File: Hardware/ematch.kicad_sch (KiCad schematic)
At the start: 34 parts, among them J3 Conn_01x02_Male, J4 Conn_01x02_Male, J5 Conn_01x02_Male, J6 Conn_01x02_Male, Q1 PMV20ENR, Q2 PMV20ENR, Q3 PMV20ENR, Q4 PMV20ENR, U6 LTV-247

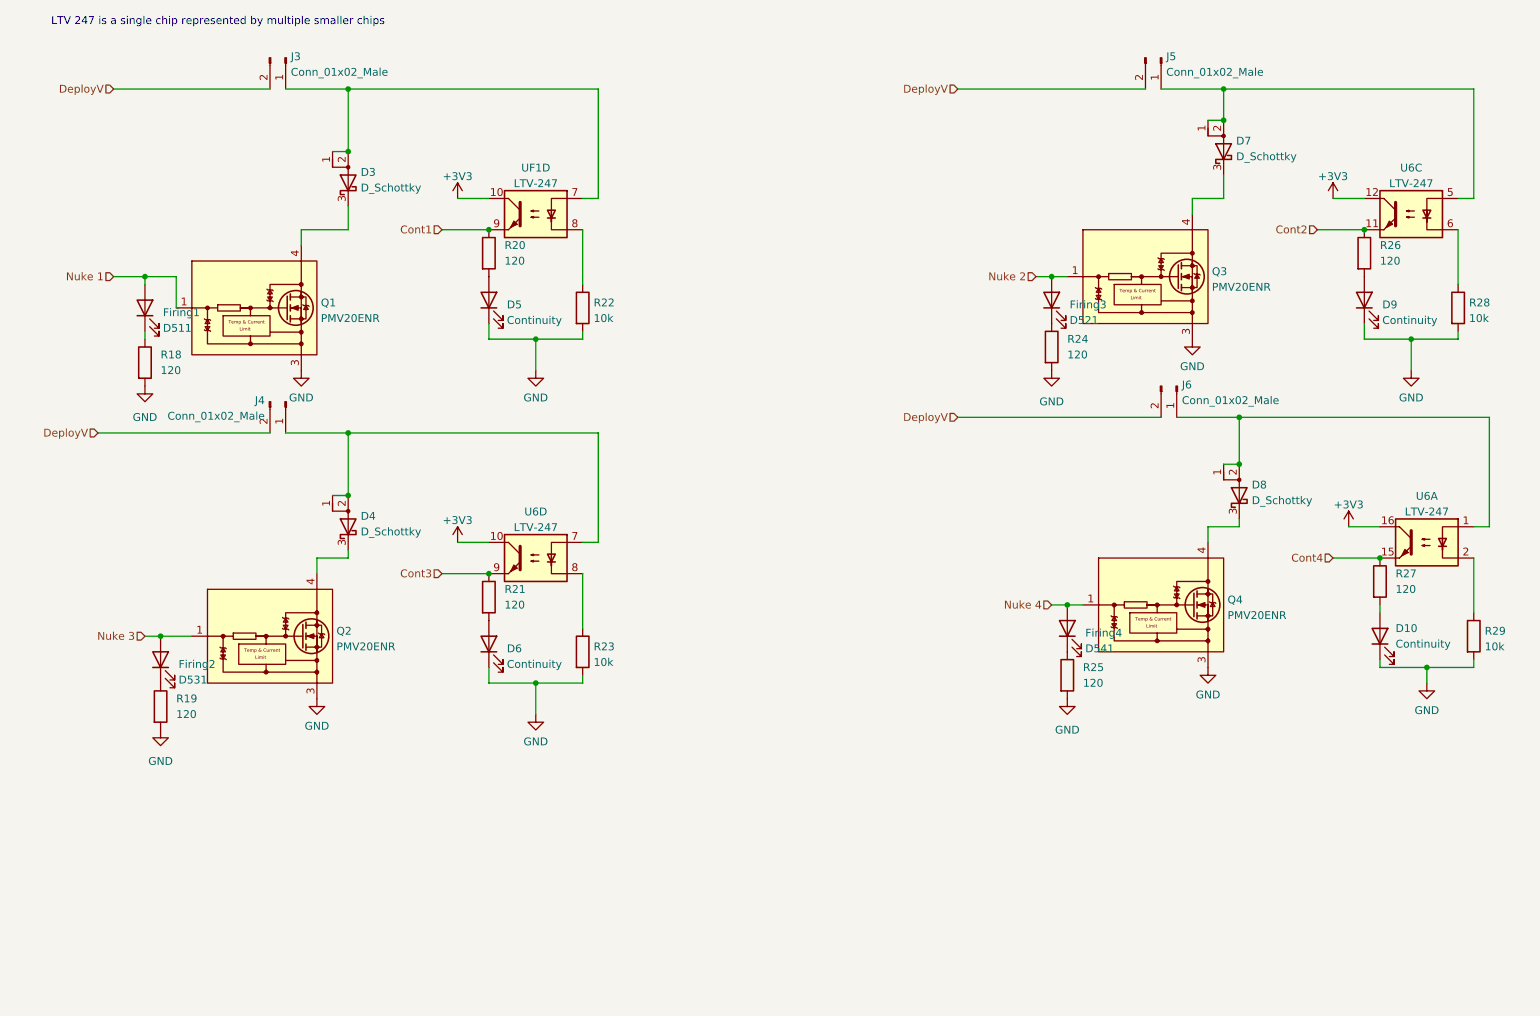
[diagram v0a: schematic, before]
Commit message: schematic done? + footprints assigned
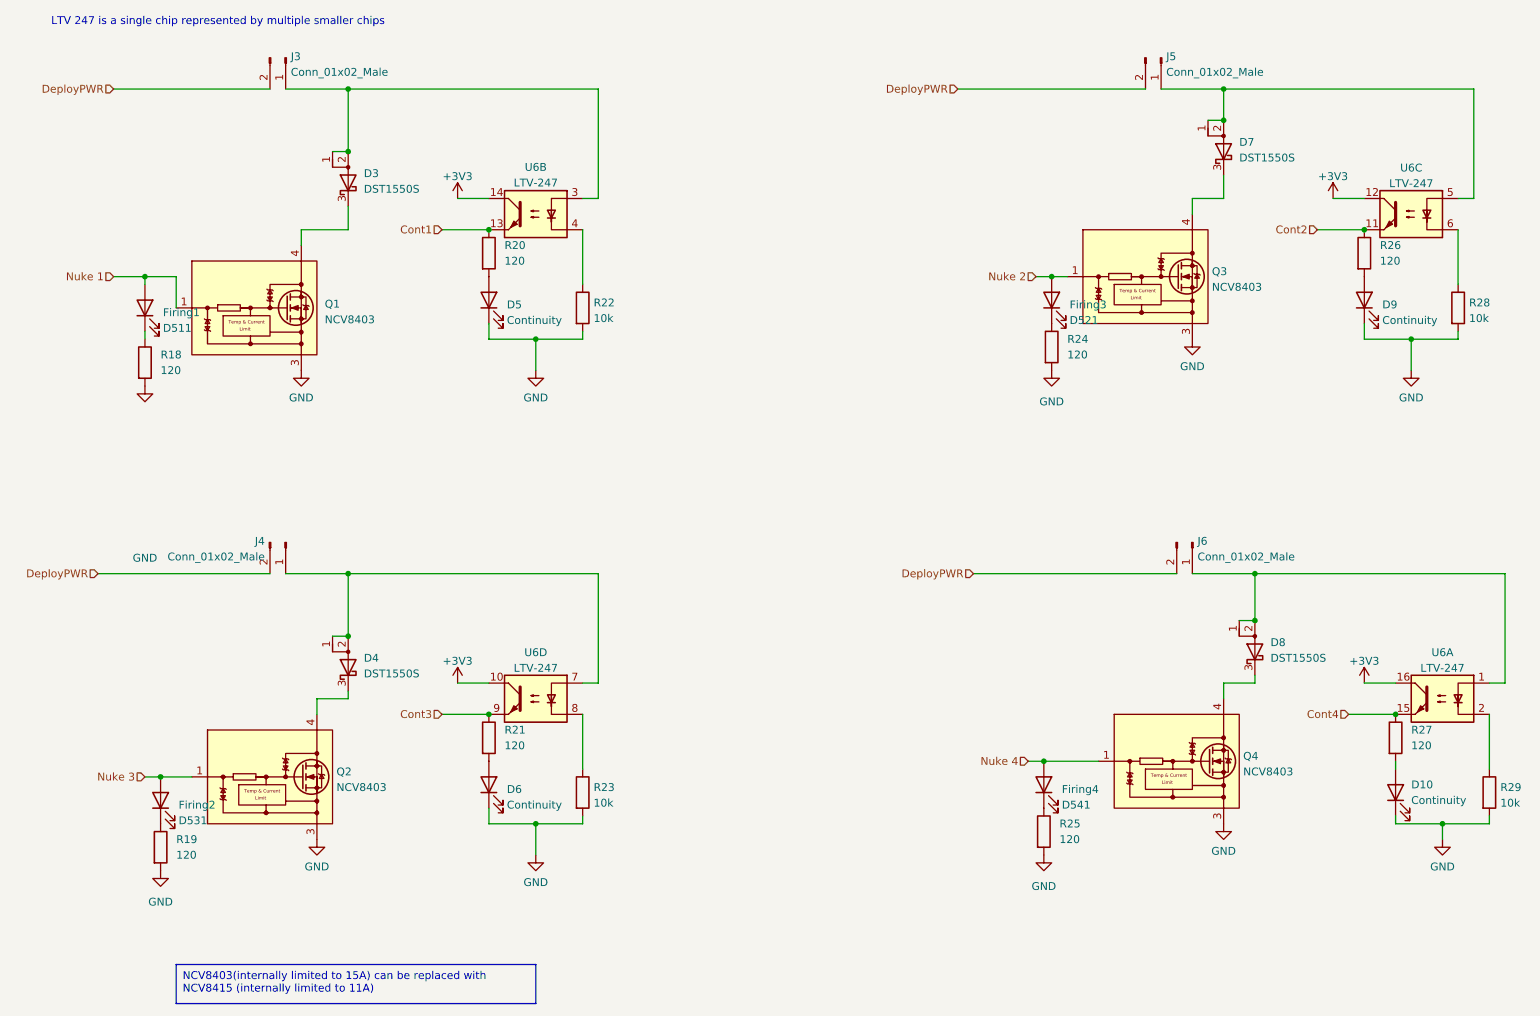
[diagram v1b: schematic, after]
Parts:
- D3, D4, D7, D8: value D_Schottky -> DST1550S
- Q1, Q2, Q3, Q4: value PMV20ENR -> NCV8403
- renumbered UF1 to U6
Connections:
- net +3V3: now also U6.14; no longer U6.10
- net Cont1: now also U6.13; no longer U6.9
- net at D3.1 (A), D3.2 (A), J3.1 (Pin_1): now also U6.3; no longer U6.7
- net at R22.1: now also U6.4; no longer U6.8
- net DeployV renamed DeployPWR
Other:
- moved on the sheet: D10, D4, D6, D8, Firing2, Firing4, J4, J6, Q2, Q4, R19, R21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

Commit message: High power side nearly done
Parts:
- J3, J4, J5, J6: footprint TerminalBlock_TE-Connectivity:TerminalBlock_TE_282834-2_1x02_P2.54mm_Horizontal -> TerminalBlock_Phoenix:TerminalBlock_Phoenix_PT-1,5-2-3.5-H_1x02_P3.50mm_Horizontal
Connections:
- net DeployPWR: now also J3.1 (Pin_1), J4.1 (Pin_1), J5.1 (Pin_1), J6.1 (Pin_1); no longer J3.2 (Pin_2), J4.2 (Pin_2), J5.2 (Pin_2), J6.2 (Pin_2)
- net at D3.1 (A), D3.2 (A), U6.3: now also J3.2 (Pin_2); no longer J3.1 (Pin_1)
- net at D4.1 (A), D4.2 (A), U6.7: now also J4.2 (Pin_2); no longer J4.1 (Pin_1)
- net at D8.1 (A), D8.2 (A), U6.1: now also J6.2 (Pin_2); no longer J6.1 (Pin_1)
- net at D7.1 (A), D7.2 (A), U6.5: now also J5.2 (Pin_2); no longer J5.1 (Pin_1)
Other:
- moved on the sheet: J3, J4, J5, J6
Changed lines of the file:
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@@
-    (stroke (width 0) (type default))
-  )
-  (wire (pts (xy 203.2 109.22) (xy 213.36 109.22))
     (stroke (width 0) (type default))
   )
@@
     (stroke (width 0) (type default))
   )
-  (wire (pts (xy 198.12 30.48) (xy 208.28 30.48))
-    (stroke (width 0) (type default))
-  )
   (wire (pts (xy 251.46 132.08) (xy 251.46 140.97))
     (stroke (width 0) (type default))
@@
     (stroke (width 0) (type default))
   )
+  (wire (pts (xy 58.42 109.22) (xy 66.04 109.22))
+    (stroke (width 0) (type default))
+  )
   (wire (pts (xy 238.76 71.12) (xy 246.38 71.12))
     (stroke (width 0) (type default))
@@
     (stroke (width 0) (type default))
   )
-  (wire (pts (xy 165.1 30.48) (xy 195.58 30.48))
-    (stroke (width 0) (type default))
-  )
   (wire (pts (xy 213.36 109.22) (xy 254 109.22))
     (stroke (width 0) (type default))
@@
     (stroke (width 0) (type default))
   )
+  (wire (pts (xy 205.74 109.22) (xy 213.36 109.22))
+    (stroke (width 0) (type default))
+  )
   (wire (pts (xy 58.42 53.34) (xy 58.42 55.88))
     (stroke (width 0) (type default))
@@
     (stroke (width 0) (type default))
   )
-  (wire (pts (xy 167.64 109.22) (xy 200.66 109.22))
-    (stroke (width 0) (type default))
-  )
-  (wire (pts (xy 55.88 109.22) (xy 66.04 109.22))
+  (wire (pts (xy 167.64 109.22) (xy 203.2 109.22))
     (stroke (width 0) (type default))
   )
@@
     (stroke (width 0) (type default))
   )
-  (wire (pts (xy 27.94 30.48) (xy 53.34 30.48))
+  (wire (pts (xy 27.94 30.48) (xy 55.88 30.48))
     (stroke (width 0) (type default))
   )
@@
     (stroke (width 0) (type default))
   )
+  (wire (pts (xy 200.66 30.48) (xy 208.28 30.48))
+    (stroke (width 0) (type default))
+  )
   (wire (pts (xy 88.9 149.86) (xy 96.52 149.86))
     (stroke (width 0) (type default))
@@
     (stroke (width 0) (type default))
   )
+  (wire (pts (xy 58.42 30.48) (xy 66.04 30.48))
+    (stroke (width 0) (type default))
+  )
   (wire (pts (xy 104.14 132.08) (xy 104.14 140.97))
     (stroke (width 0) (type default))
@@
     (stroke (width 0) (type default))
   )
-  (wire (pts (xy 25.4 109.22) (xy 53.34 109.22))
+  (wire (pts (xy 25.4 109.22) (xy 55.88 109.22))
     (stroke (width 0) (type default))
   )
@@
     (stroke (width 0) (type default))
   )
-  (wire (pts (xy 55.88 30.48) (xy 66.04 30.48))
-    (stroke (width 0) (type default))
-  )
   (wire (pts (xy 63.5 119.38) (xy 66.04 119.38))
     (stroke (width 0) (type default))
   )
   (wire (pts (xy 228.6 132.08) (xy 236.22 132.08))
+    (stroke (width 0) (type default))
+  )
+  (wire (pts (xy 165.1 30.48) (xy 198.12 30.48))
     (stroke (width 0) (type default))
   )
@@
     )
   )
-  (symbol (lib_id "Connector:Conn_01x02_Male") (at 55.88 25.4 270) (unit 1)
-    (in_bom yes) (on_board yes) (dnp no) (fields_autoplaced)
-    (property "Reference" "J3" (at 56.7182 25.2003 90)
-      (effects (font (size 1.27 1.27)) (justify left))
-    )
-    (property "Value" "Conn_01x02_Male" (at 56.7182 27.7372 90)
-      (effects (font (size 1.27 1.27)) (justify left))
-    )
-    (property "Footprint" "TerminalBlock_TE-Connectivity:TerminalBlock_TE_282834-2_1x02_P2.54mm_Horizontal" (at 55.88 25.4 0)
+  (symbol (lib_id "Connector:Conn_01x02_Male") (at 55.88 25.4 90) (mirror x) (unit 1)
+    (in_bom yes) (on_board yes) (dnp no)
+    (property "Reference" "J3" (at 55.0418 25.2003 90)
+      (effects (font (size 1.27 1.27)) (justify left))
+    )
+    (property "Value" "Conn_01x02_Male" (at 55.0418 27.7372 90)
+      (effects (font (size 1.27 1.27)) (justify left))
+    )
+    (property "Footprint" "TerminalBlock_Phoenix:TerminalBlock_Phoenix_PT-1,5-2-3.5-H_1x02_P3.50mm_Horizontal" (at 55.88 25.4 0)
       (effects (font (size 1.27 1.27)) hide)
     )
@@
     )
   )
-  (symbol (lib_id "Connector:Conn_01x02_Male") (at 55.88 104.14 270) (unit 1)
+  (symbol (lib_id "Connector:Conn_01x02_Male") (at 55.88 104.14 90) (mirror x) (unit 1)
     (in_bom yes) (on_board yes) (dnp no)
-    (property "Reference" "J4" (at 52.5019 103.9403 90)
-      (effects (font (size 1.27 1.27)) (justify right))
-    )
-    (property "Value" "Conn_01x02_Male" (at 52.5019 106.4772 90)
-      (effects (font (size 1.27 1.27)) (justify right))
-    )
-    (property "Footprint" "TerminalBlock_TE-Connectivity:TerminalBlock_TE_282834-2_1x02_P2.54mm_Horizontal" (at 55.88 104.14 0)
+    (property "Reference" "J4" (at 59.2581 103.9403 90)
+      (effects (font (size 1.27 1.27)) (justify right))
+    )
+    (property "Value" "Conn_01x02_Male" (at 59.2581 106.4772 90)
+      (effects (font (size 1.27 1.27)) (justify right))
+    )
+    (property "Footprint" "TerminalBlock_Phoenix:TerminalBlock_Phoenix_PT-1,5-2-3.5-H_1x02_P3.50mm_Horizontal" (at 55.88 104.14 0)
       (effects (font (size 1.27 1.27)) hide)
     )
@@
     )
   )
-  (symbol (lib_id "Connector:Conn_01x02_Male") (at 198.12 25.4 270) (unit 1)
-    (in_bom yes) (on_board yes) (dnp no) (fields_autoplaced)
-    (property "Reference" "J5" (at 198.9582 25.2003 90)
-      (effects (font (size 1.27 1.27)) (justify left))
-    )
-    (property "Value" "Conn_01x02_Male" (at 198.9582 27.7372 90)
-      (effects (font (size 1.27 1.27)) (justify left))
-    )
-    (property "Footprint" "TerminalBlock_TE-Connectivity:TerminalBlock_TE_282834-2_1x02_P2.54mm_Horizontal" (at 198.12 25.4 0)
+  (symbol (lib_id "Connector:Conn_01x02_Male") (at 198.12 25.4 90) (mirror x) (unit 1)
+    (in_bom yes) (on_board yes) (dnp no)
+    (property "Reference" "J5" (at 205.74 21.5931 90)
+      (effects (font (size 1.27 1.27)) (justify left))
+    )
+    (property "Value" "Conn_01x02_Male" (at 205.74 24.13 90)
+      (effects (font (size 1.27 1.27)) (justify left))
+    )
+    (property "Footprint" "TerminalBlock_Phoenix:TerminalBlock_Phoenix_PT-1,5-2-3.5-H_1x02_P3.50mm_Horizontal" (at 198.12 25.4 0)
       (effects (font (size 1.27 1.27)) hide)
     )
@@
     )
   )
-  (symbol (lib_id "Connector:Conn_01x02_Male") (at 203.2 104.14 270) (unit 1)
-    (in_bom yes) (on_board yes) (dnp no) (fields_autoplaced)
-    (property "Reference" "J6" (at 204.0382 103.9403 90)
-      (effects (font (size 1.27 1.27)) (justify left))
-    )
-    (property "Value" "Conn_01x02_Male" (at 204.0382 106.4772 90)
-      (effects (font (size 1.27 1.27)) (justify left))
-    )
-    (property "Footprint" "TerminalBlock_TE-Connectivity:TerminalBlock_TE_282834-2_1x02_P2.54mm_Horizontal" (at 203.2 104.14 0)
-      (effects (font (size 1.27 1.27)) hide)
-    )
+  (symbol (lib_id "Connector:Conn_01x02_Male") (at 203.2 104.14 90) (mirror x) (unit 1)
+    (in_bom yes) (on_board yes) (dnp no)
+    (property "Reference" "J6" (at 205.74 99.06 90)
+      (effects (font (size 1.27 1.27)) (justify left))
+    )
+    (property "Value" "Conn_01x02_Male" (at 209.55 101.6 90)
+      (effects (font (size 1.27 1.27)) (justify left))
+    )
+    (property "Footprint" "TerminalBlock_Phoenix:TerminalBlock_Phoenix_PT-1,5-2-3.5-H_1x02_P3.50mm_Horizontal" (at 203.2 104.14 0)
+      (effects (font (size 1.27 1.27)) hide)
+    )
